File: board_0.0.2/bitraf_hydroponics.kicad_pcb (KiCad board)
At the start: 2 copper layers, 67.3 x 86.4 mm, 36 parts, among them P1 12V_PWR, P10 ROT_BTN, P11 BUZZ, P12 LDR, P13 MOS_OUT_2, P14 MOS_OUT_1, P15 MOS_OUT_3, P17 BREAKOUT_1-15, P18 BREAKOUT_16-30, P2 I2C_1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

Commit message: fixed Vin bug. Traced new route for buzz and ldr. Added resistors to terminals
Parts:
- added R1: 4.7k, Resistors_ThroughHole:Resistor_Horizontal_RM10mm, F.Cu at (256.5, 137.2)
- added R6: 4.7k, Resistors_ThroughHole:Resistor_Horizontal_RM10mm, F.Cu at (256.5, 108.0)
- added R7: 4.7k, Resistors_ThroughHole:Resistor_Horizontal_RM10mm, F.Cu at (256.5, 124.5)
- R3, R4, R5: value R -> 10k
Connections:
- P17 pad 1: +3V3 -> +5V
- P17 pad 5: Net-(P17-Pad5) -> +3V3
- U1 pad 1: +3V3 -> +5V
- U1 pad 5: Net-(P17-Pad5) -> +3V3
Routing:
- net +5V: track 65.9 -> 108.2 mm
- net +3V3: track 72.7 -> 103.2 mm
- net GND: track 443.5 -> 428.4 mm
- net Net-(P17-Pad5): track 2.54 -> 0.00 mm

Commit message: moved i2c bus out of the way for USB and rerouted. Also removed resistors over terminals
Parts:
- removed R1, R6, R7: 4.7k, Resistors_ThroughHole:Resistor_Horizontal_RM10mm
- moved P7 19.8 mm to (198.1, 146.1), turned to 270 degrees
- moved P4 15.9 mm to (198.1, 142.2), turned to 270 degrees
- moved P5 12.7 mm to (190.5, 160.0)
- moved P3 12.3 mm to (198.1, 138.4), turned to 270 degrees
- moved P9 12.3 mm to (198.1, 130.8), turned to 270 degrees
- moved P2 9.69 mm to (198.1, 134.6), turned to 270 degrees
- moved P11 7.73 mm to (176.5, 147.3)
- moved P10 7.62 mm to (198.1, 160.0)
- moved P12 7.62 mm to (182.9, 160.0)
- moved R2 7.62 mm to (182.9, 154.9)
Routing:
- net +5V: track 108.2 -> 135.2 mm
- net GND: track 428.4 -> 405.7 mm
- net /TEMP_HUM: track 45.6 -> 56.6 mm
- net /LDR_PIN: track 79.3 -> 89.7 mm
- net /BUZZ: track 70.4 -> 80.5 mm
- net +3V3: track 103.2 -> 112.7 mm
- net /ROT_SW: track 55.0 -> 62.6 mm
- net /ROT_1: track 49.5 -> 56.7 mm
- net /ROT_0: track 43.2 -> 50.1 mm
- net /SDA: track 66.4 -> 71.3 mm
- net /SCL: track 72.3 -> 73.4 mm
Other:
- board text added: "5+"
- board text added: "GND"
- board text added: "SCL"
- board text added: "SDA"

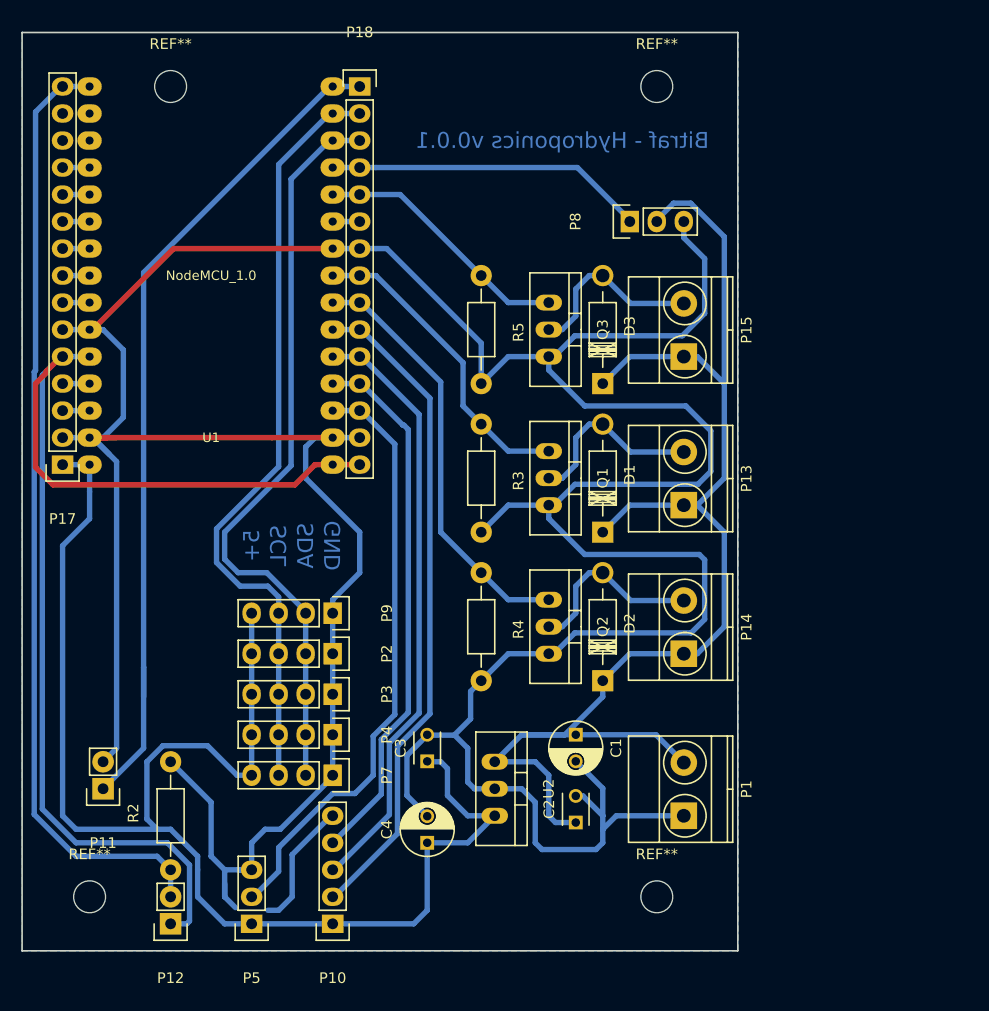
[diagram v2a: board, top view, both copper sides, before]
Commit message: pcb: not exactly sure what I did, but it passes the tests. Models: tweaked to work with the low kuggis bed. New dome fits perfectly over stand pipe
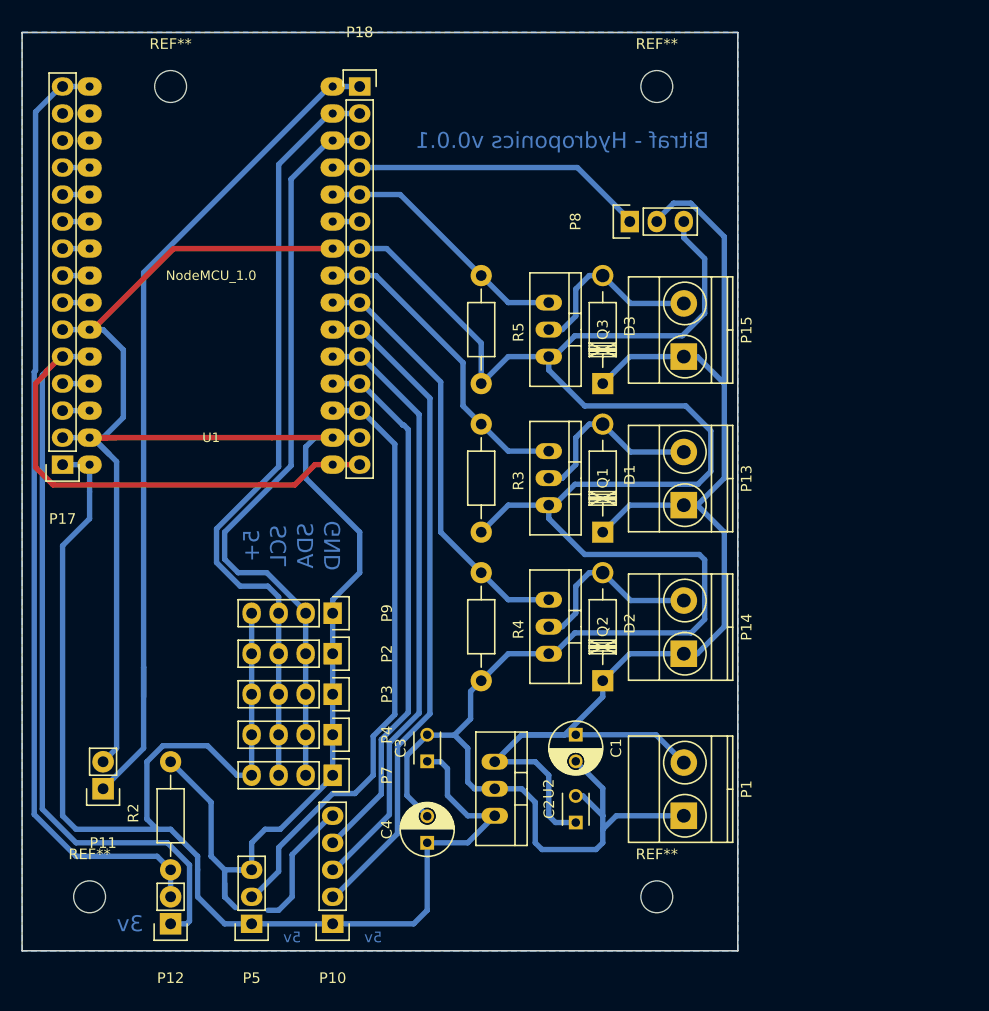
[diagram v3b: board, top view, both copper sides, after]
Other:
- board text added: "3v"
- board text added: "5v"
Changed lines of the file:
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@@
-(kicad_pcb (version 4) (host pcbnew 4.0.2+dfsg1-stable)
+(kicad_pcb (version 4) (host pcbnew 4.0.7-e2-6376~58~ubuntu16.04.1)
   (general
     (links 105)
     (no_connects 0)
-    (area 168.834999 76.124999 236.295001 162.635001)
+    (area 156.925001 69.275 238.169 166.249)
     (thickness 1.6)
-    (drawings 11)
+    (drawings 14)
     (tracks 347)
     (zones 0)
@@
     (fp_circle (center 0 0) (end 3 0) (layer Cmts.User) (width 0.381))
     (pad 1 thru_hole circle (at 0 0) (size 3 3) (drill 3) (layers))
+  )
+  (gr_text 3v (at 179.07 160.02) (layer B.Cu)
+    (effects (font (size 1.5 1.5) (thickness 0.3)) (justify mirror))
+  )
+  (gr_text 5v (at 201.93 161.29) (layer B.Cu)
+    (effects (font (size 1 1) (thickness 0.25)) (justify mirror))
+  )
+  (gr_text 5v (at 194.31 161.29) (layer B.Cu)
+    (effects (font (size 1 1) (thickness 0.25)) (justify mirror))
   )
   (gr_text GND (at 198.12 124.46 90) (layer B.Cu)
@@
     (polygon
       (pts
+        (xy 168.91 76.2) (xy 236.22 76.2) (xy 236.22 162.56) (xy 168.91 162.56)
+      )
+    )
+  )
+  (zone (net 2) (net_name GND) (layer B.Cu) (hatch edge 0.508)
+    (connect_pads (clearance 0.508))
+    (min_thickness 0.254)
+    (fill yes (arc_segments 16) (thermal_gap 0.508) (thermal_bridge_width 0.508))
+    (polygon
+      (pts

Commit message: o Refreshing footprints with updated KiCAD libraries. All parts have 3D-models now except the NodeMCU. o Adding some more text on the copper. o Fixing a couple of ERC warnings.
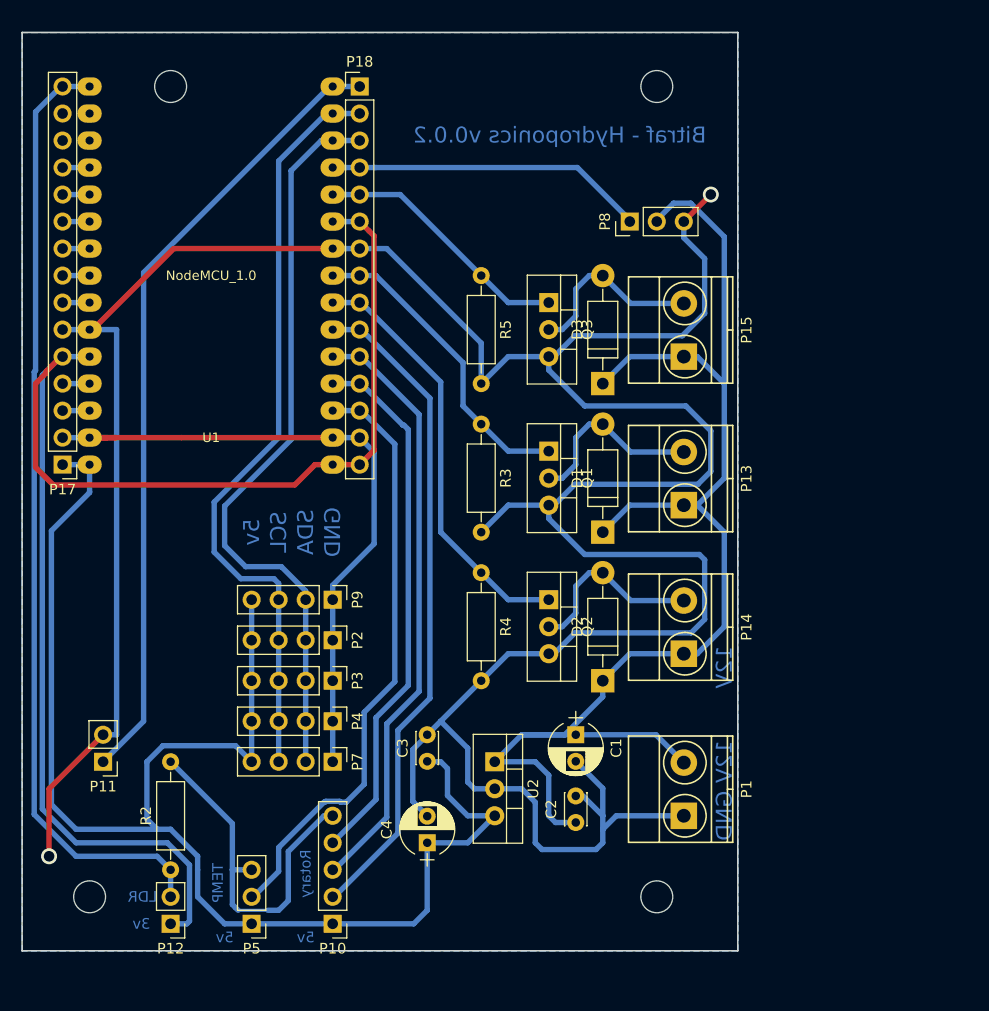
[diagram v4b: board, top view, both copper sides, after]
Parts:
- C1, C4: footprint Capacitors_ThroughHole:C_Radial_D5_L6_P2.5 -> Capacitors_THT:CP_Radial_D5.0mm_P2.50mm
- C2, C3: footprint Capacitors_ThroughHole:C_Disc_D3_P2.5 -> Capacitors_THT:C_Disc_D3.0mm_W2.0mm_P2.50mm
- D1, D2, D3: footprint Diodes_ThroughHole:Diode_DO-41_SOD81_Horizontal_RM10 -> Diodes_THT:D_DO-41_SOD81_P10.16mm_Horizontal
- P10: footprint Pin_Headers:Pin_Header_Straight_1x05 -> Pin_Headers:Pin_Header_Straight_1x05_Pitch2.54mm
- P11, P12: footprint Pin_Headers:Pin_Header_Straight_1x02 -> Pin_Headers:Pin_Header_Straight_1x02_Pitch2.54mm
- P17, P18: footprint Pin_Headers:Pin_Header_Straight_1x15 -> Pin_Headers:Pin_Header_Straight_1x15_Pitch2.54mm
- P2, P3, P4, P7, P9: footprint Pin_Headers:Pin_Header_Straight_1x04 -> Pin_Headers:Pin_Header_Straight_1x04_Pitch2.54mm
- P5, P8: footprint Pin_Headers:Pin_Header_Straight_1x03 -> Pin_Headers:Pin_Header_Straight_1x03_Pitch2.54mm
- Q1, Q2, Q3, U2: footprint TO_SOT_Packages_THT:TO-220_Neutral123_Vertical -> TO_SOT_Packages_THT:TO-220_Vertical
- R2, R3, R4, R5: footprint Resistors_ThroughHole:Resistor_Horizontal_RM10mm -> Resistors_THT:R_Axial_DIN0207_L6.3mm_D2.5mm_P10.16mm_Horizontal
- moved Q2 2.54 mm to (218.4, 129.5)
- moved Q1 2.54 mm to (218.4, 115.6)
- moved Q3 2.54 mm to (218.4, 101.6)
- moved P11 2.54 mm to (176.5, 144.8)
- moved U2 2.54 mm to (213.4, 144.8)
- moved P2 1.27 mm to (198.1, 133.3)
- moved P3 1.27 mm to (198.1, 137.2)
- moved P4 1.27 mm to (198.1, 141.0)
- moved P7 1.27 mm to (198.1, 144.8)
- moved P9 1.27 mm to (198.1, 129.5)
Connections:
- P18 pad 6: Net-(P18-Pad6) -> +3V3
- U1 pad 21: Net-(P18-Pad6) -> +3V3
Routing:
- net +3V3: track 112.7 -> 139.2 mm
- net GND: track 405.7 -> 399.1 mm, vias 0 -> 2
- net /BUZZ: track 80.5 -> 75.2 mm
- net Net-(P18-Pad6): track 2.54 -> 0.00 mm
- net /SCL: track 73.4 -> 72.8 mm
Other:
- net class Default: via_dia 0.6 -> 1.5; via_drill 0.4 -> 1
- rule via_min_drill: 0.3 -> 1
- rule via_min_size: 0.4 -> 1.5
- board text added: "12V"
- board text added: "Bitraf - Hydroponics v0.0.2"
- board text added: "LDR"
- board text added: "Rotary"
- board text added: "TEMP"
- board text removed: "5+"
- board text removed: "Bitraf - Hydroponics v0.0.1"
